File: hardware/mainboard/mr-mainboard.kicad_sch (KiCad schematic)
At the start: 0 parts

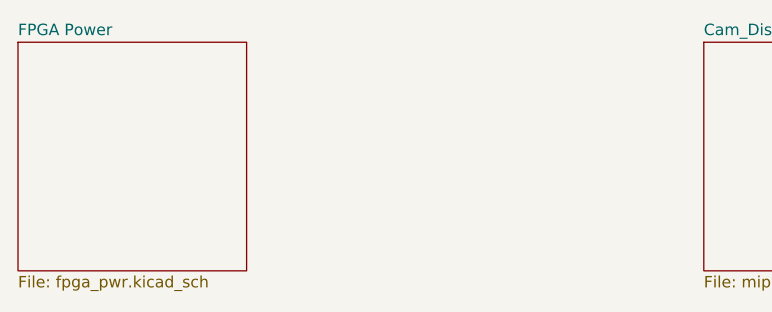
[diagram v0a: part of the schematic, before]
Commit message: FPGA IO planning
Signed-off-by: David Shah <dave@ds0.me>
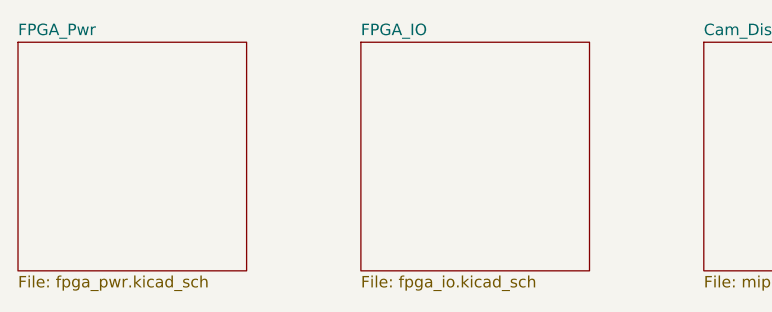
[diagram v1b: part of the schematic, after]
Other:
- sheet FPGA Power renamed FPGA_Pwr
- added sheet FPGA_IO (fpga_io.kicad_sch)
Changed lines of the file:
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@@
+    )
+  )
+  (sheet (at 76.2 38.1) (size 25.4 25.4)
+    (stroke (width 0.001) (type solid) (color 132 0 132 1))
+    (fill (color 255 255 255 0.0000))
+    (property "Sheet name" "FPGA_IO" (id 0) (at 76.2 37.4641 0)
+      (effects (font (size 1.27 1.27)) (justify left bottom))
+    )
+    (property "Sheet file" "fpga_io.kicad_sch" (id 1) (at 76.2 64.0089 0)
+      (effects (font (size 1.27 1.27)) (justify left top))
     )
   )
@@
     (stroke (width 0.001) (type solid) (color 132 0 132 1))
     (fill (color 255 255 255 0.0000))
-    (property "Sheet name" "FPGA Power" (id 0) (at 38.1 37.4641 0)
+    (property "Sheet name" "FPGA_Pwr" (id 0) (at 38.1 37.4641 0)
       (effects (font (size 1.27 1.27)) (justify left bottom))
     )
@@
     (path "/7dd540ee-d364-4396-a5ce-94105f298dc9/" (page "2"))
     (path "/926b833a-4cee-458d-ad7a-784832562e66/" (page "3"))
+    (path "/23c4d1b8-430f-47fa-afd5-87283c046e16/" (page "4"))
   )
   (symbol_instances
@@
       (reference "U?") (unit 11) (value "LIFCL_40_CABGA400") (footprint "")
     )
-  )
+    (path "/23c4d1b8-430f-47fa-afd5-87283c046e16/324e0f2b-39a0-4982-963a-c6ec960c0405"
+      (reference "#PWR?") (unit 1) (value "+3V3") (footprint "")
+    )
+    (path "/23c4d1b8-430f-47fa-afd5-87283c046e16/44312dc7-d919-4cca-a927-0f1e07e0f224"
+      (reference "#PWR?") (unit 1) (value "+1V8") (footprint "")
+    )
+    (path "/23c4d1b8-430f-47fa-afd5-87283c046e16/79c8e6ec-0590-45d3-9bc0-bf8a44f86c55"
+      (reference "#PWR?") (unit 1) (value "GND") (footprint "")
+    )
+    (path "/23c4d1b8-430f-47fa-afd5-87283c046e16/7a57862b-e25a-48d4-bee9-bfd6da57578a"
+      (reference "#PWR?") (unit 1) (value "GND") (footprint "")
+    )
+    (path "/23c4d1b8-430f-47fa-afd5-87283c046e16/8a03643c-482d-4de4-bc60-fd74eccf2543"
+      (reference "#PWR?") (unit 1) (value "+3V3") (footprint "")
+    )
+    (path "/23c4d1b8-430f-47fa-afd5-87283c046e16/92c7a6e4-f182-4e4a-bf02-e5591a804c6b"
+      (reference "#PWR?") (unit 1) (value "+3V3") (footprint "")
+    )
+    (path "/23c4d1b8-430f-47fa-afd5-87283c046e16/98e4e951-7576-4fb1-9035-6832fce8aceb"
+      (reference "#PWR?") (unit 1) (value "+1V5") (footprint "")
+    )
+    (path "/23c4d1b8-430f-47fa-afd5-87283c046e16/e145986f-ea5e-4ecf-9e55-67a4ebb67069"
+      (reference "#PWR?") (unit 1) (value "+3V3") (footprint "")
+    )
+    (path "/23c4d1b8-430f-47fa-afd5-87283c046e16/f94844d2-cf8a-47e5-851b-3e727fb926fd"
+      (reference "#PWR?") (unit 1) (value "GND") (footprint "")
+    )
+    (path "/23c4d1b8-430f-47fa-afd5-87283c046e16/fbacf117-a396-4115-9d34-845a1032961b"
+      (reference "#PWR?") (unit 1) (value "GND") (footprint "")
+    )
+    (path "/23c4d1b8-430f-47fa-afd5-87283c046e16/117eedfa-c39c-4ebc-88ae-2ade2b30b5cf"
+      (reference "C?") (unit 1) (value "10µ") (footprint "")
+    )
+    (path "/23c4d1b8-430f-47fa-afd5-87283c046e16/307bf316-24b0-45e1-bafd-e64607bdff0a"
+      (reference "C?") (unit 1) (value "470n") (footprint "")
+    )
+    (path "/23c4d1b8-430f-47fa-afd5-87283c046e16/3896bbcf-3afc-4c43-8dfa-7e3990175c2c"
+      (reference "C?") (unit 1) (value "470n") (footprint "")
+    )
+    (path "/23c4d1b8-430f-47fa-afd5-87283c046e16/3d74ef8b-6774-4e88-9d04-9b8c48f747c5"
+      (reference "C?") (unit 1) (value "470n") (footprint "")
+    )
+    (path "/23c4d1b8-430f-47fa-afd5-87283c046e16/453be04c-a5aa-467e-a355-ea07b019618c"
+      (reference "C?") (unit 1) (value "470n") (footprint "")
+    )
+    (path "/23c4d1b8-430f-47fa-afd5-87283c046e16/4f2d6f91-37b4-4613-8877-7726e31ac850"
+      (reference "C?") (unit 1) (value "10µ") (footprint "")
+    )
+    (path "/23c4d1b8-430f-47fa-afd5-87283c046e16/96499cb5-7fe5-46ce-b066-0285c24bc1b3"
+      (reference "C?") (unit 1) (value "470n") (footprint "")
+    )
+    (path "/23c4d1b8-430f-47fa-afd5-87283c046e16/c3e868c8-a792-4280-a100-75cf43f603dc"
+      (reference "C?") (unit 1) (value "10µ") (footprint "")
+    )
+    (path "/23c4d1b8-430f-47fa-afd5-87283c046e16/d5a8eb67-0040-47f0-a149-e03a21d6d0ce"
+      (reference "C?") (unit 1) (value "470n") (footprint "")
+    )
+    (path "/23c4d1b8-430f-47fa-afd5-87283c046e16/f2568583-1f3b-4f8d-a228-1a4b45952794"
+      (reference "C?") (unit 1) (value "10µ") (footprint "")
+    )
+    (path "/23c4d1b8-430f-47fa-afd5-87283c046e16/30c6f721-eca5-4d3f-9a25-06feb0b115ec"
+      (reference "R?") (unit 1) (value "4.7k") (footprint "")
+    )
+    (path "/23c4d1b8-430f-47fa-afd5-87283c046e16/36b7571b-f87b-48aa-ba48-062335c59c70"
+      (reference "R?") (unit 1) (value "4.7k") (footprint "")
+    )
+    (path "/23c4d1b8-430f-47fa-afd5-87283c046e16/5551df14-d716-4e63-9c28-11e1ecb598dd"
+      (reference "R?") (unit 1) (value "4.7k") (footprint "")
+    )
+    (path "/23c4d1b8-430f-47fa-afd5-87283c046e16/687f1acc-375f-4163-b32a-5cfd0f25b8c6"
+      (reference "R?") (unit 1) (value "4.7k") (footprint "")
+    )
+    (path "/23c4d1b8-430f-47fa-afd5-87283c046e16/99fe03bb-2e53-4d7c-a792-16fe6b2670f9"
+      (reference "R?") (unit 1) (value "4.7k") (footprint "")
+    )
+    (path "/23c4d1b8-430f-47fa-afd5-87283c046e16/00219b54-2431-44ec-a9cc-39dd12d81bb6"
+      (reference "U?") (unit 2) (value "LIFCL_40_CABGA400") (footprint "")
+    )
+    (path "/23c4d1b8-430f-47fa-afd5-87283c046e16/67def79e-148a-4ea5-b8e0-6dfa0f8a859d"
+      (reference "U?") (unit 3) (value "LIFCL_40_CABGA400") (footprint "")
+    )
+    (path "/23c4d1b8-430f-47fa-afd5-87283c046e16/34e49a0a-8dc3-4df6-aa2b-a1506f842e3e"
+      (reference "U?") (unit 4) (value "LIFCL_40_CABGA400") (footprint "")
+    )
+    (path "/23c4d1b8-430f-47fa-afd5-87283c046e16/f349093c-f8a5-465c-84d5-df4ae82a9e47"
+      (reference "U?") (unit 5) (value "LIFCL_40_CABGA400") (footprint "")
+    )
+    (path "/23c4d1b8-430f-47fa-afd5-87283c046e16/977f388a-cf05-4c10-a247-0edd4e0bc24a"
+      (reference "U?") (unit 6) (value "LIFCL_40_CABGA400") (footprint "")
+    )
+    (path "/23c4d1b8-430f-47fa-afd5-87283c046e16/c69fdcc2-44fe-44c3-92b6-205eaec4bee3"
+      (reference "U?") (unit 7) (value "LIFCL_40_CABGA400") (footprint "")
+    )
+    (path "/23c4d1b8-430f-47fa-afd5-87283c046e16/dac3958b-4dab-4dc1-97c5-4c7f0e9e54b9"
+      (reference "U?") (unit 8) (value "LIFCL_40_CABGA400") (footprint "")
+    )
+    (path "/23c4d1b8-430f-47fa-afd5-87283c046e16/d012b94c-d7e6-4da0-bfb9-f1988389810d"
+      (reference "U?") (unit 9) (value "LIFCL_40_CABGA400") (footprint "")
+    )
+  )

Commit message: Connecting up various bits
Signed-off-by: David Shah <dave@ds0.me>
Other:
- added sheet Connectors (conn.kicad_sch)
- added sheet Misc (misc.kicad_sch)
- added sheet Power (power.kicad_sch)

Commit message: More stuff
Signed-off-by: David Shah <dave@ds0.me>
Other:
- added sheet DRAM (dram.kicad_sch)

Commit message: Working on layout
Signed-off-by: David Shah <dave@ds0.me>
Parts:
- added H1, H2, H3, H4: MountingHole, MountingHole:MountingHole_2.7mm_M2.5, symbol Mechanical:MountingHole
- added H5: MountingHole, meowality:9774025151R, symbol Mechanical:MountingHole
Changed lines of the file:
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@@
 (kicad_sch (version 20210126) (generator eeschema)
   (paper "A4")
+  (symbol (lib_id "Mechanical:MountingHole") (at 215.9 63.5 0) (unit 1)
+    (in_bom yes) (on_board yes)
+    (property "Reference" "H1" (id 0) (at 218.4401 62.3506 0)
+      (effects (font (size 1.27 1.27)) (justify left))
+    )
+    (property "Value" "MountingHole" (id 1) (at 218.4401 64.6493 0)
+      (effects (font (size 1.27 1.27)) (justify left))
+    )
+    (property "Footprint" "MountingHole:MountingHole_2.7mm_M2.5" (id 2) (at 215.9 63.5 0)
+      (effects (font (size 1.27 1.27)) hide)
+    )
+    (property "Datasheet" "~" (id 3) (at 215.9 63.5 0)
+      (effects (font (size 1.27 1.27)) hide)
+    )
+  )
+  (symbol (lib_id "Mechanical:MountingHole") (at 215.9 69.85 0) (unit 1)
+    (in_bom yes) (on_board yes)
+    (property "Reference" "H2" (id 0) (at 218.4401 68.7006 0)
+      (effects (font (size 1.27 1.27)) (justify left))
+    )
+    (property "Value" "MountingHole" (id 1) (at 218.4401 70.9993 0)
+      (effects (font (size 1.27 1.27)) (justify left))
+    )
+    (property "Footprint" "MountingHole:MountingHole_2.7mm_M2.5" (id 2) (at 215.9 69.85 0)
+      (effects (font (size 1.27 1.27)) hide)
+    )
+    (property "Datasheet" "~" (id 3) (at 215.9 69.85 0)
+      (effects (font (size 1.27 1.27)) hide)
+    )
+  )
+  (symbol (lib_id "Mechanical:MountingHole") (at 215.9 74.93 0) (unit 1)
+    (in_bom yes) (on_board yes)
+    (property "Reference" "H3" (id 0) (at 218.4401 73.7806 0)
+      (effects (font (size 1.27 1.27)) (justify left))
+    )
+    (property "Value" "MountingHole" (id 1) (at 218.4401 76.0793 0)
+      (effects (font (size 1.27 1.27)) (justify left))
+    )
+    (property "Footprint" "MountingHole:MountingHole_2.7mm_M2.5" (id 2) (at 215.9 74.93 0)
+      (effects (font (size 1.27 1.27)) hide)
+    )
+    (property "Datasheet" "~" (id 3) (at 215.9 74.93 0)
+      (effects (font (size 1.27 1.27)) hide)
+    )
+  )
+  (symbol (lib_id "Mechanical:MountingHole") (at 215.9 81.28 0) (unit 1)
+    (in_bom yes) (on_board yes)
+    (property "Reference" "H4" (id 0) (at 218.4401 80.1306 0)
+      (effects (font (size 1.27 1.27)) (justify left))
+    )
+    (property "Value" "MountingHole" (id 1) (at 218.4401 82.4293 0)
+      (effects (font (size 1.27 1.27)) (justify left))
+    )
+    (property "Footprint" "MountingHole:MountingHole_2.7mm_M2.5" (id 2) (at 215.9 81.28 0)
+      (effects (font (size 1.27 1.27)) hide)
+    )
+    (property "Datasheet" "~" (id 3) (at 215.9 81.28 0)
+      (effects (font (size 1.27 1.27)) hide)
+    )
+  )
+  (symbol (lib_id "Mechanical:MountingHole") (at 215.9 88.9 0) (unit 1)
+    (in_bom yes) (on_board yes)
+    (property "Reference" "H5" (id 0) (at 218.4401 87.7506 0)
+      (effects (font (size 1.27 1.27)) (justify left))
+    )
+    (property "Value" "MountingHole" (id 1) (at 218.4401 90.0493 0)
+      (effects (font (size 1.27 1.27)) (justify left))
+    )
+    (property "Footprint" "meowality:9774025151R" (id 2) (at 215.9 88.9 0)
+      (effects (font (size 1.27 1.27)) hide)
+    )
+    (property "Datasheet" "~" (id 3) (at 215.9 88.9 0)
+      (effects (font (size 1.27 1.27)) hide)
+    )
+  )
   (sheet (at 114.3 38.1) (size 25.4 25.4)
     (stroke (width 0.001) (type solid) (color 132 0 132 1))
@@
   )
   (symbol_instances
+    (path "/2a727066-23b2-42f4-88da-4f7a020b89b2"
+      (reference "H1") (unit 1) (value "MountingHole") (footprint "MountingHole:MountingHole_2.7mm_M2.5")
+    )
+    (path "/fc4ecb81-0f51-4040-adf5-7e03fcfc8710"
+      (reference "H2") (unit 1) (value "MountingHole") (footprint "MountingHole:MountingHole_2.7mm_M2.5")
+    )
+    (path "/710b30eb-77ed-4d74-a17c-e1969039ca62"
+      (reference "H3") (unit 1) (value "MountingHole") (footprint "MountingHole:MountingHole_2.7mm_M2.5")
+    )
+    (path "/39218fa2-549f-495c-977f-2517a7785a2b"
+      (reference "H4") (unit 1) (value "MountingHole") (footprint "MountingHole:MountingHole_2.7mm_M2.5")
+    )
+    (path "/a5d91f34-d2a0-4453-93ad-825a450a8ddb"
+      (reference "H5") (unit 1) (value "MountingHole") (footprint "meowality:9774025151R")
+    )
     (path "/7dd540ee-d364-4396-a5ce-94105f298dc9/4dd6052b-4c44-4337-bca1-1febcef57c4e"
       (reference "#PWR01") (unit 1) (value "GND") (footprint "")
@@
     )
     (path "/fab76c53-3adb-4867-b007-ffb14aef2f22/1f28fc80-5e32-4c90-8262-fb490a2e71b9"
-      (reference "J3") (unit 1) (value "EAR") (footprint "Connector_PinHeader_2.54mm:PinHeader_2x03_P2.54mm_Horizontal")
+      (reference "J3") (unit 1) (value "EAR") (footprint "Connector_PinHeader_2.00mm:PinHeader_2x03_P2.00mm_Horizontal")
     )
     (path "/fab76c53-3adb-4867-b007-ffb14aef2f22/03adfbf0-11f4-4773-98d0-8b49bcac8472"
@@
       (reference "R26") (unit 1) (value "10k") (footprint "Resistor_SMD:R_0402_1005Metric")
     )
-    (path "/fab76c53-3adb-4867-b007-ffb14aef2f22/b0efb6e7-77d4-48b3-90d5-8ce2ee293e5d"
-      (reference "R27") (unit 1) (value "10k") (footprint "Resistor_SMD:R_0402_1005Metric")
-    )
     (path "/fab76c53-3adb-4867-b007-ffb14aef2f22/66fe7f9b-8d05-4724-aaa2-93952a700c19"
       (reference "R28") (unit 1) (value "10k") (footprint "Resistor_SMD:R_0402_1005Metric")
@@
       (reference "SW1") (unit 1) (value "SW_Push") (footprint "Button_Switch_THT:SW_Tactile_SPST_Angled_PTS645Vx31-2LFS")
     )
-    (path "/fab76c53-3adb-4867-b007-ffb14aef2f22/11249cce-8d50-4594-ac41-e1138b1e2a24"
+    (path "/fab76c53-3adb-4867-b007-ffb14aef2f22/7334a4b3-93c3-48c5-b0b3-231670f445fd"
       (reference "SW2") (unit 1) (value "SW_Push") (footprint "Button_Switch_THT:SW_Tactile_SPST_Angled_PTS645Vx31-2LFS")
     )
-    (path "/fab76c53-3adb-4867-b007-ffb14aef2f22/7334a4b3-93c3-48c5-b0b3-231670f445fd"
-      (reference "SW3") (unit 1) (value "SW_Push") (footprint "Button_Switch_THT:SW_Tactile_SPST_Angled_PTS645Vx31-2LFS")
-    )
     (path "/fab76c53-3adb-4867-b007-ffb14aef2f22/5ef466bb-b771-4c4a-8164-fe0f34a373fa"
